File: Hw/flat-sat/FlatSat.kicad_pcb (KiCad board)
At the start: 4 copper layers, 48 x 32 mm, 106 parts, among them J1 Antenna, J2 Antenna, J3 periphs, J4 SWD, P1 USB_C_Plug_USB2.0, U1 TLV75733PDBVR, U10 LIS2DH, U11 BME280 /BMP280, U2 0900FM15D0039, U3 PE42421, U4 SX1262IMLTRT, U5 W25Q16JV, U6 0900FM15D0039, U7 PE42421, U8 SX1262IMLTRT, U9 RP2040, Y1 32Mhz, Y2 32Mhz, Y3 12MHz

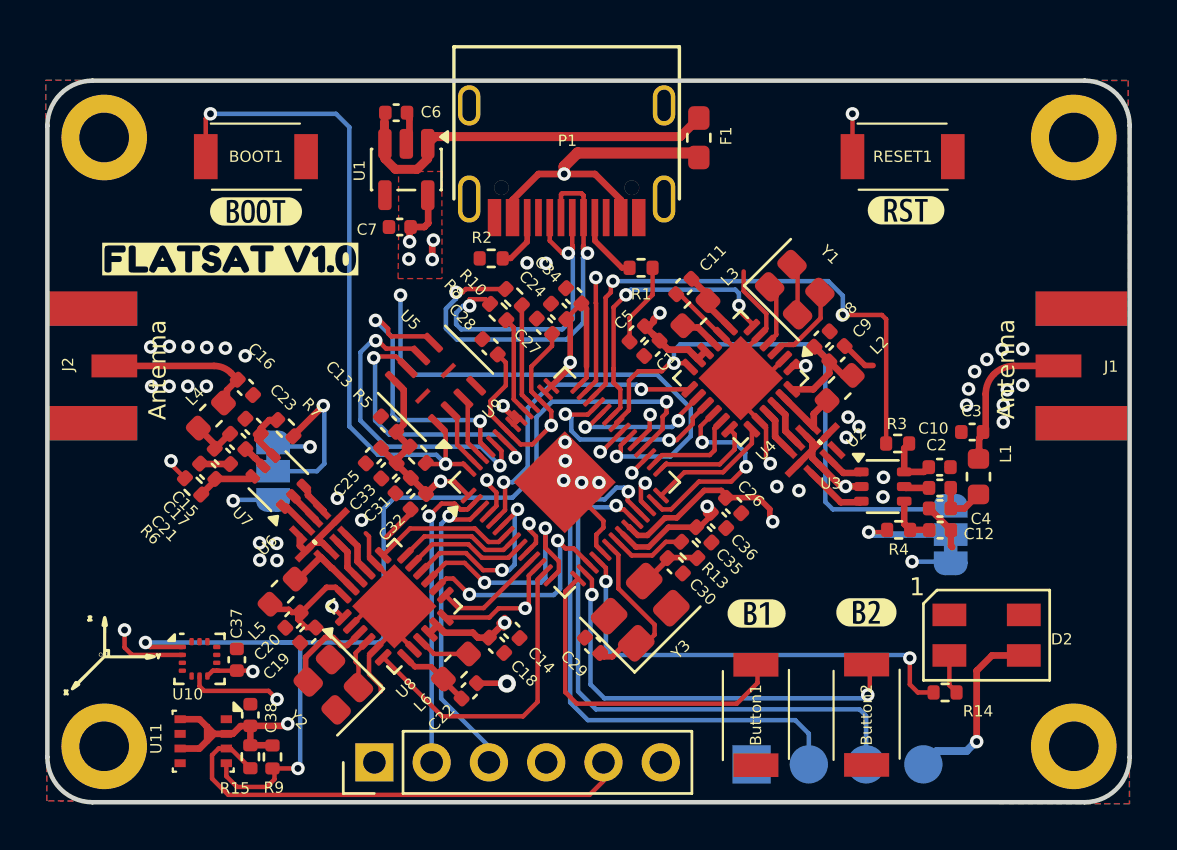
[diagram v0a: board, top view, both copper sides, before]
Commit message: feat(Hw):Update_BoM
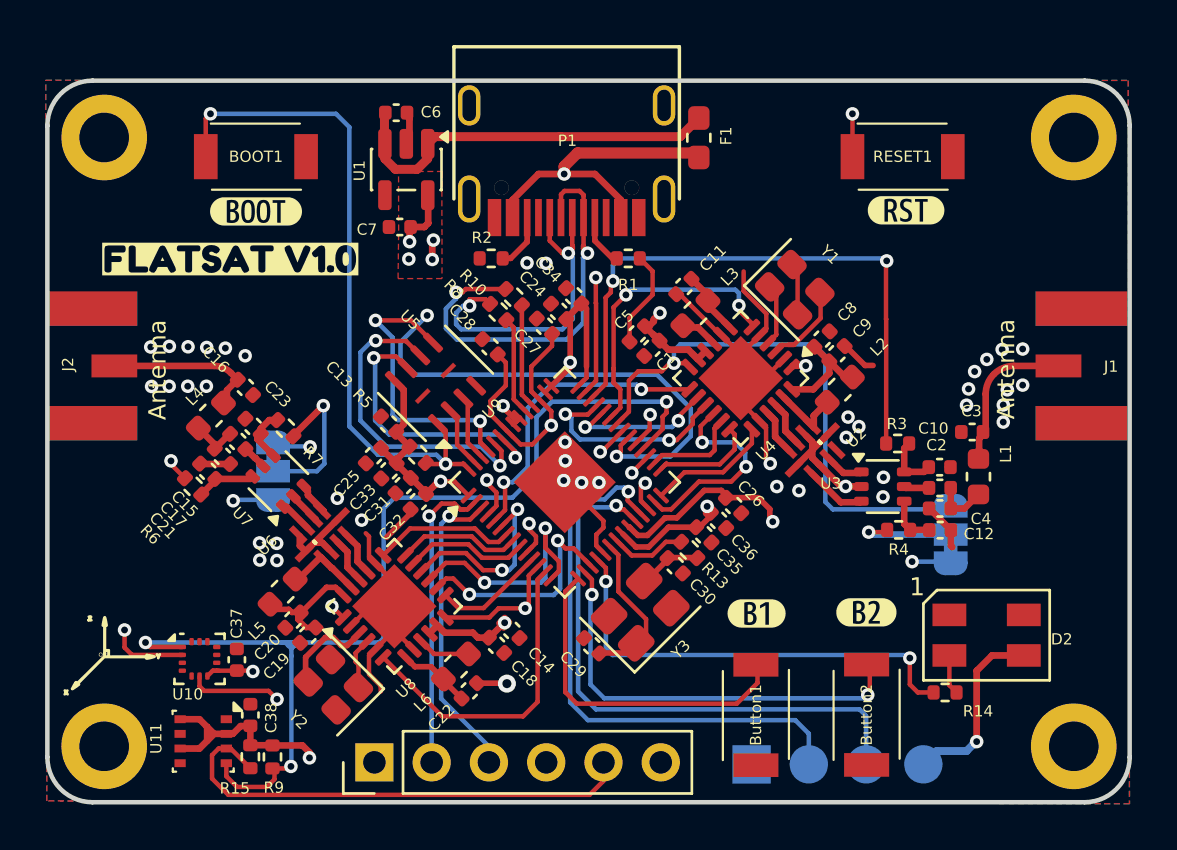
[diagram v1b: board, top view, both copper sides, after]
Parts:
- moved R1 0.70 mm to (104.5, 102.9)
- moved L2 0.07 mm to (113.9, 108.7)
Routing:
- net /SDA: track 71.6 -> 74.5 mm
- net /R0_ANT_SW: track 24.5 -> 26.8 mm
- net /INT1: track 49.6 -> 51.7 mm
- net /SCL: track 71.9 -> 70.6 mm
- net Net-(P1-CC): track 3.06 -> 2.32 mm
- net /DIO23: track 21.4 -> 22.1 mm
- net Net-(U9-XIN): track 7.68 -> 6.95 mm
- net GND: track 62.0 -> 62.7 mm

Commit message: Fix(Hw): update RF floorplan
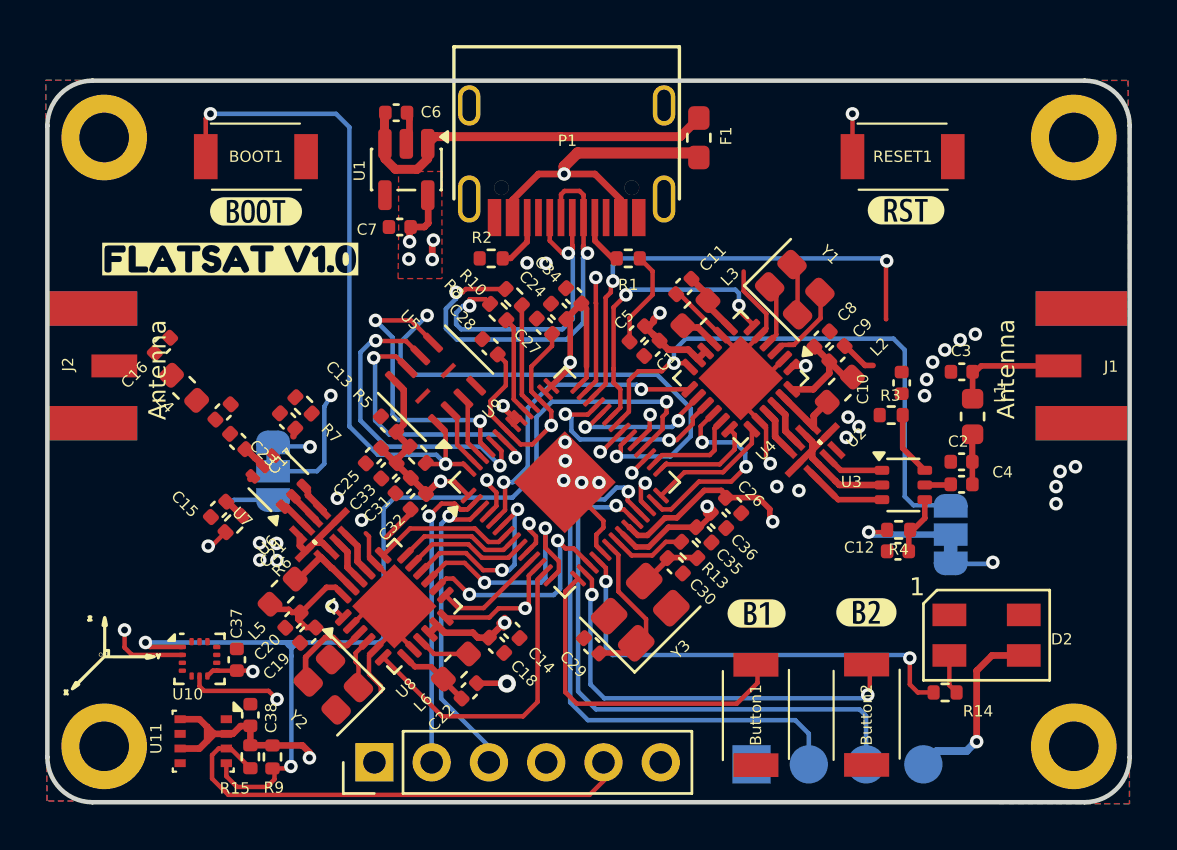
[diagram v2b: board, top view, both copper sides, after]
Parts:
- moved C16 4.12 mm to (83.8, 106.7), turned to 45 degrees
- moved C10 4.10 mm to (116.6, 108.4), turned to 90 degrees
- moved C3 2.71 mm to (119.3, 107.9)
- moved L1 2.68 mm to (119.8, 109.9)
- moved R6 2.45 mm to (87.0, 114.7), turned to -135 degrees
- moved C4 2.28 mm to (119.3, 111.9)
- moved C12 2.09 mm to (116.5, 115.9), turned to 180 degrees
- moved C17 1.97 mm to (86.5, 109.7), turned to 45 degrees
- moved C21 1.76 mm to (86.3, 114.0), turned to -135 degrees
- moved L4 1.71 mm to (84.8, 108.6), turned to -45 degrees
- moved C23 1.55 mm to (89.4, 110.1), turned to -45 degrees
- moved R7 1.29 mm to (90.1, 109.4)
- moved R3 1.29 mm to (116.2, 109.8)
- moved C2 0.98 mm to (119.3, 112.9)
- moved U3 0.92 mm to (116.7, 112.9)
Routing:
- net Net-(J2-In): track 6.98 -> 0.01 mm
- net /DIO2: track 25.6 -> 31.3 mm
- net /R0_ANT_SW: track 26.8 -> 21.2 mm
- net GND: track 62.7 -> 59.8 mm, vias 43 -> 30
- net Net-(U7-V2): track 2.45 -> 0.00 mm
- net Net-(C15-Pad2): track 2.18 -> 0.02 mm
- net Net-(J1-In): track 6.94 -> 5.11 mm
- net Net-(U7-V1): track 2.66 -> 1.11 mm
- net Net-(JP2-C): track 6.92 -> 5.52 mm
- net Net-(C2-Pad2): track 2.40 -> 3.43 mm
- net Net-(U2-SW_RFI): track 2.81 -> 3.65 mm
- net Net-(U2-SW_RFO): track 1.85 -> 2.70 mm
- net /R1_DIO2: vias 2 -> 1

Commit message: fix(Hw):Floorplan_Updated
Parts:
- moved R7 2.73 mm to (88.7, 111.8), turned to 0 degrees
- moved C16 2.66 mm to (86.2, 107.9), turned to 0 degrees
- moved C15 2.57 mm to (85.8, 113.2), turned to 90 degrees
- moved C17 2.10 mm to (86.3, 111.8), turned to 0 degrees
- moved C18 1.98 mm to (99.5, 121.8)
- moved C14 1.95 mm to (100.1, 121.2)
- moved R6 1.83 mm to (87.1, 116.5), turned to 180 degrees
- moved C21 1.74 mm to (87.1, 115.5), turned to 180 degrees
- moved L4 1.58 mm to (85.8, 109.8), turned to -90 degrees
- moved U7 1.40 mm to (87.9, 113.7), turned to 180 degrees
- moved U8 1.00 mm to (94.8, 119.0)
- moved C23 0.96 mm to (88.7, 110.8), turned to 0 degrees
- moved L5 0.93 mm to (90.0, 118.1), turned to 135 degrees
- moved U6 0.89 mm to (92.3, 115.0)
- moved C22 0.86 mm to (98.2, 122.5)
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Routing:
- net /R1_ANT_SW: track 32.0 -> 37.6 mm
- net Net-(J2-In): track 0.01 -> 5.31 mm
- net /R0_ANT_SW: track 21.2 -> 25.8 mm
- net Net-(U7-V2): track 0.00 -> 3.10 mm
- net +3V3: track 61.8 -> 64.8 mm
- net /INT1: track 51.7 -> 49.1 mm
- net /SCL: track 70.6 -> 68.2 mm
- net Net-(JP2-C): track 5.52 -> 3.24 mm
- net Net-(C15-Pad2): track 0.02 -> 2.13 mm
- net GND: track 59.8 -> 57.8 mm, vias 30 -> 77
- net Net-(U6-SW_RFI): track 1.53 -> 3.49 mm
- net /SDA: track 74.5 -> 76.1 mm
- net /R1_XTA: track 4.93 -> 3.57 mm
- net Net-(U7-V1): track 1.11 -> 2.45 mm
- net /R1_RFO: track 3.44 -> 4.67 mm
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
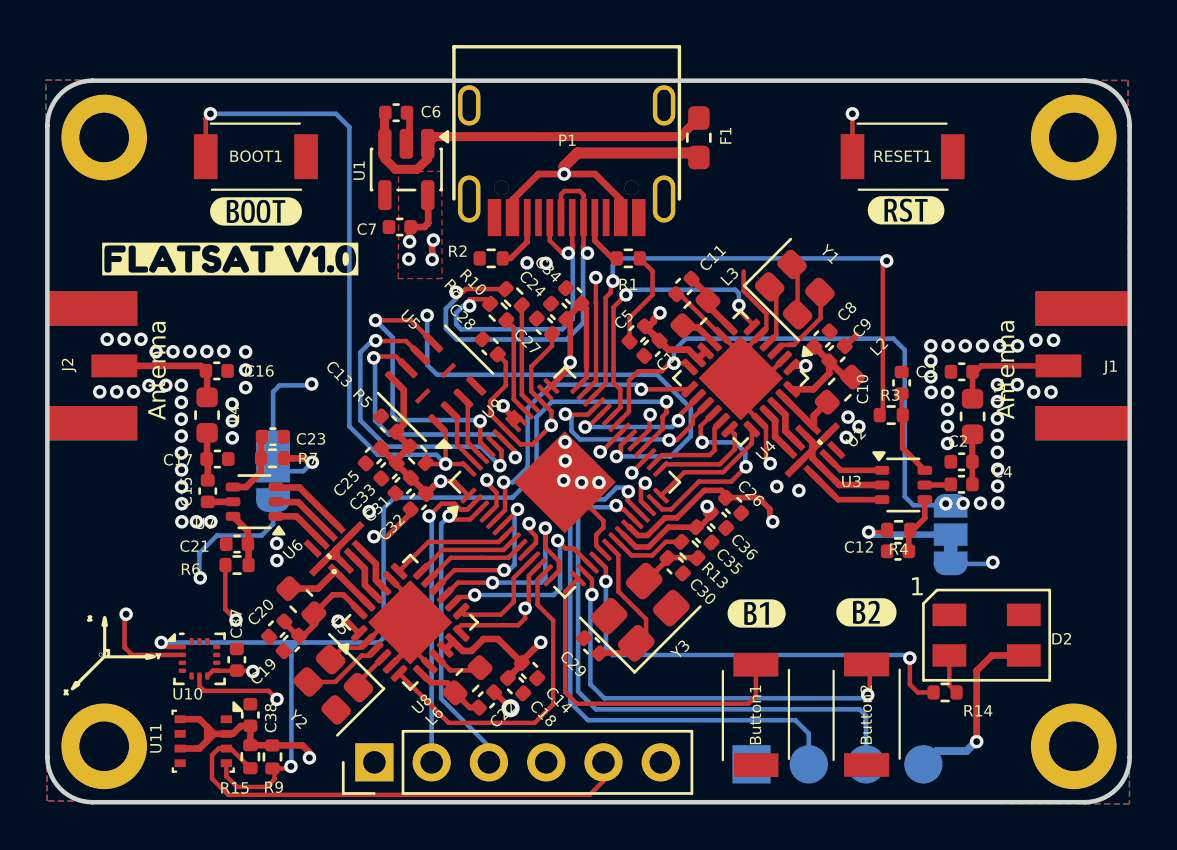
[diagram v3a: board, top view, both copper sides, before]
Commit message: fix ground plane 4 layers
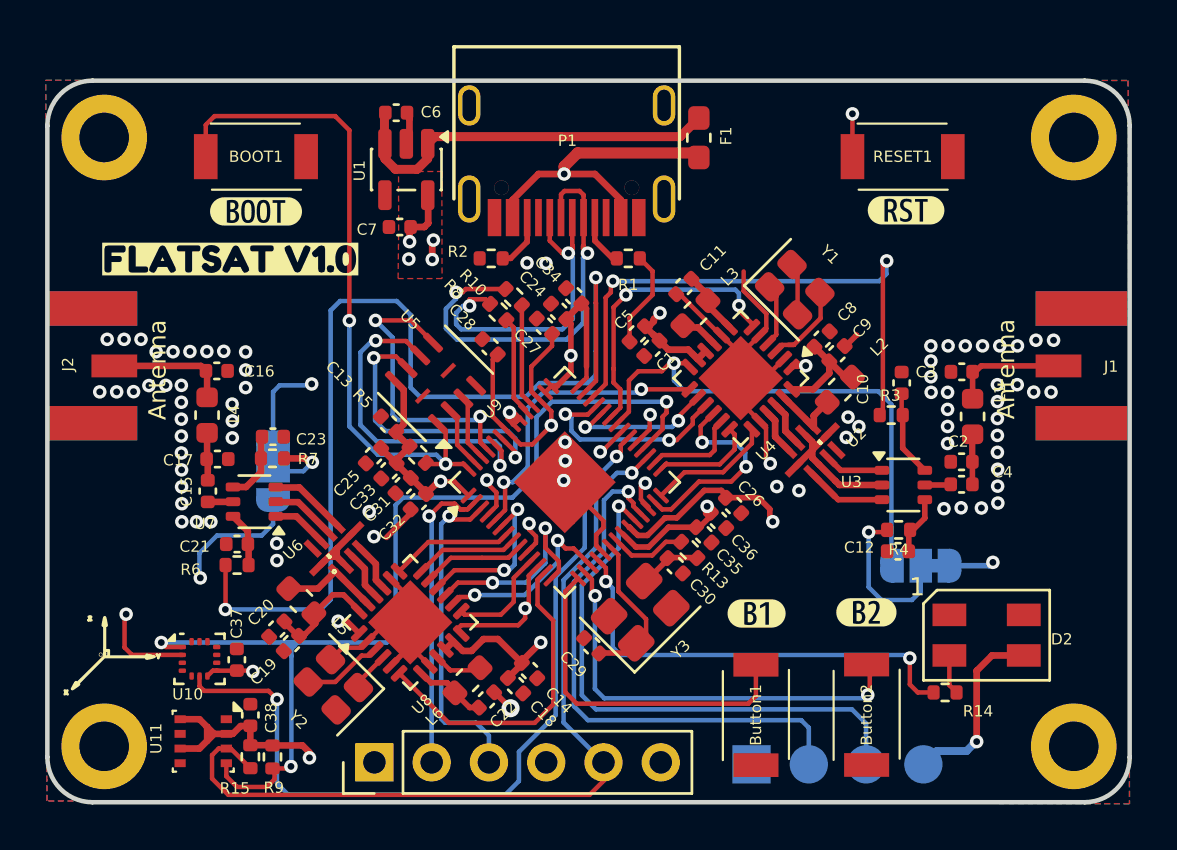
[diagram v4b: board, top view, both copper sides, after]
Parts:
- moved JP1 1.92 mm to (117.5, 116.5), turned to 180 degrees
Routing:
- net /INT1: track 49.1 -> 36.3 mm, vias 3 -> 2
- net /R1_ANT_SW: track 37.6 -> 45.3 mm
- net /SDA: track 76.1 -> 70.0 mm
- net Net-(JP1-C): track 4.54 -> 7.29 mm
- net /R0_DIO2: track 25.2 -> 23.3 mm
- net /SWCLK: track 26.3 -> 25.0 mm
- net /R1_BUSY: track 9.12 -> 8.27 mm
- net /RXD: track 13.6 -> 14.5 mm
- net /SWDIO: track 25.4 -> 24.6 mm
- net /QSPI_SCK: track 14.3 -> 15.0 mm
- net GND: vias 77 -> 75
